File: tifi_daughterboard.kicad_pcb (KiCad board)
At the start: 2 copper layers, 52.3 x 31.5 mm, 19 parts, among them J1 SSW-110-23-F-D, J2 SSW-110-23-F-D, J3 SM04B-SRSS-TB(LF)(SN), J4 SSW-103-02-T-S-RA, Q1 BSS138LT1G, U1 SGP40-D-R4, U2 SHT40-AD1B-R3

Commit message: Routing start
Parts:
- moved R5 8.72 mm to (159.3, 96.4), turned to -90 degrees
- moved D2 7.64 mm to (159.9, 89.7)
- moved Q1 7.64 mm to (156.3, 92.2)
- moved R3 7.64 mm to (156.3, 87.1)
- moved R7 5.45 mm to (131.2, 75.9)
- moved R4 4.64 mm to (160.2, 93.3), turned to 180 degrees
- moved R6 4.48 mm to (130.3, 73.4), turned to 0 degrees
- moved U1 3.95 mm to (145.1, 82.3)
- moved C3 3.75 mm to (134.0, 98.6), turned to 90 degrees
- moved C1 2.99 mm to (147.9, 83.2)
- moved C2 2.79 mm to (141.5, 83.5), turned to 0 degrees
- moved R2 2.51 mm to (142.2, 80.4), turned to -90 degrees
- moved D1 0.13 mm to (159.9, 74.7)
- turned U2 to 0 degrees
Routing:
- net +5V: track 0.00 -> 57.0 mm
- net +3.3V: track 0.00 -> 55.5 mm
- net I2C_SCL: track 17.5 -> 46.4 mm
- net I2C_SDA: track 10.3 -> 38.4 mm
- net LDR_OUT: track 0.00 -> 12.1 mm, vias 0 -> 2
- net Net-(Q1-Pad2): track 0.00 -> 7.02 mm
- net GND: track 0.00 -> 6.17 mm, vias 0 -> 1
- net Net-(U1-Pad1): track 0.00 -> 5.17 mm
- net Net-(D2-Pad2): track 0.00 -> 3.88 mm
- net Net-(D2-Pad1): track 0.00 -> 2.74 mm
- net Net-(D1-Pad2): track 0.00 -> 2.65 mm
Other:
- board size 52.3 x 31.5 mm -> 57.4 x 32.1 mm

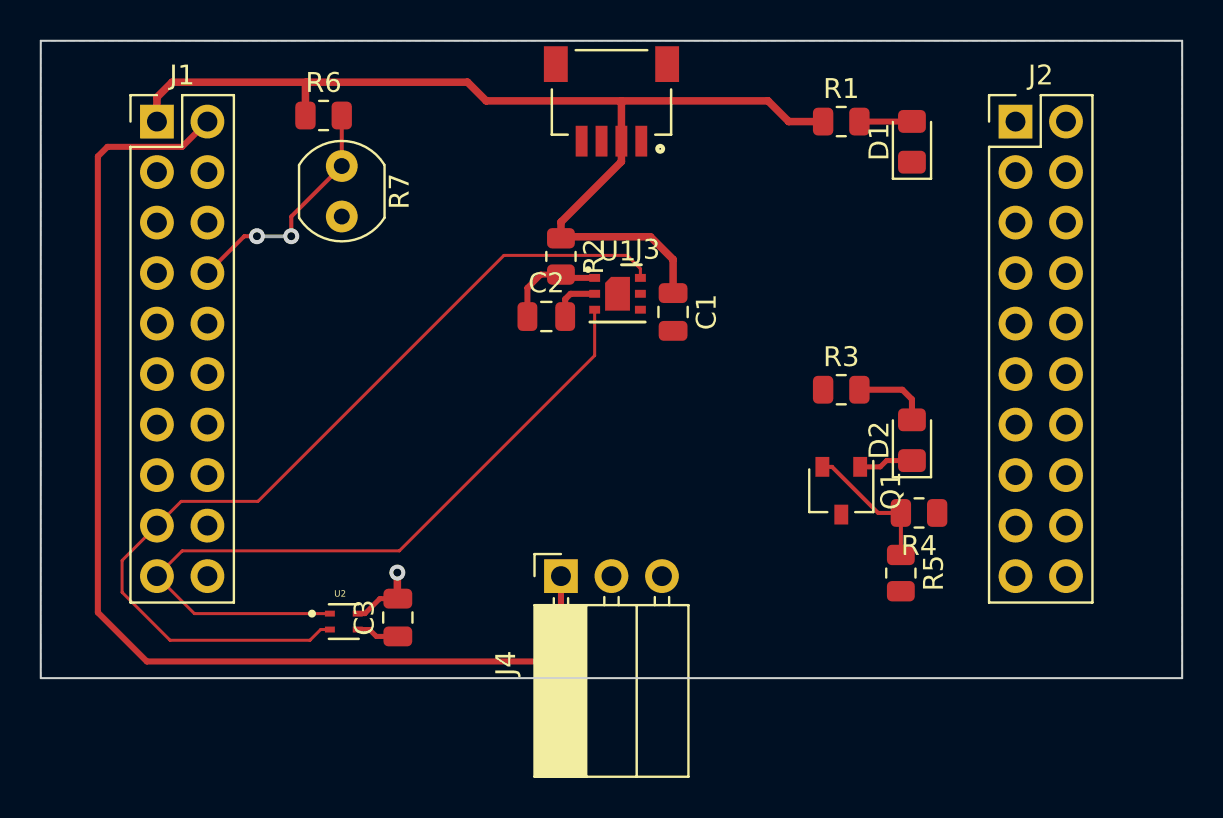
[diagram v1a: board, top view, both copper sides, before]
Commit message: Complete routing, still some TODOs.
TODOS include:
Test pads / points
Reduce vias on I2C signals?
TVS diodes on connectors
Shunt option for blue LED (bypass PWM)
Optional I2C pullups
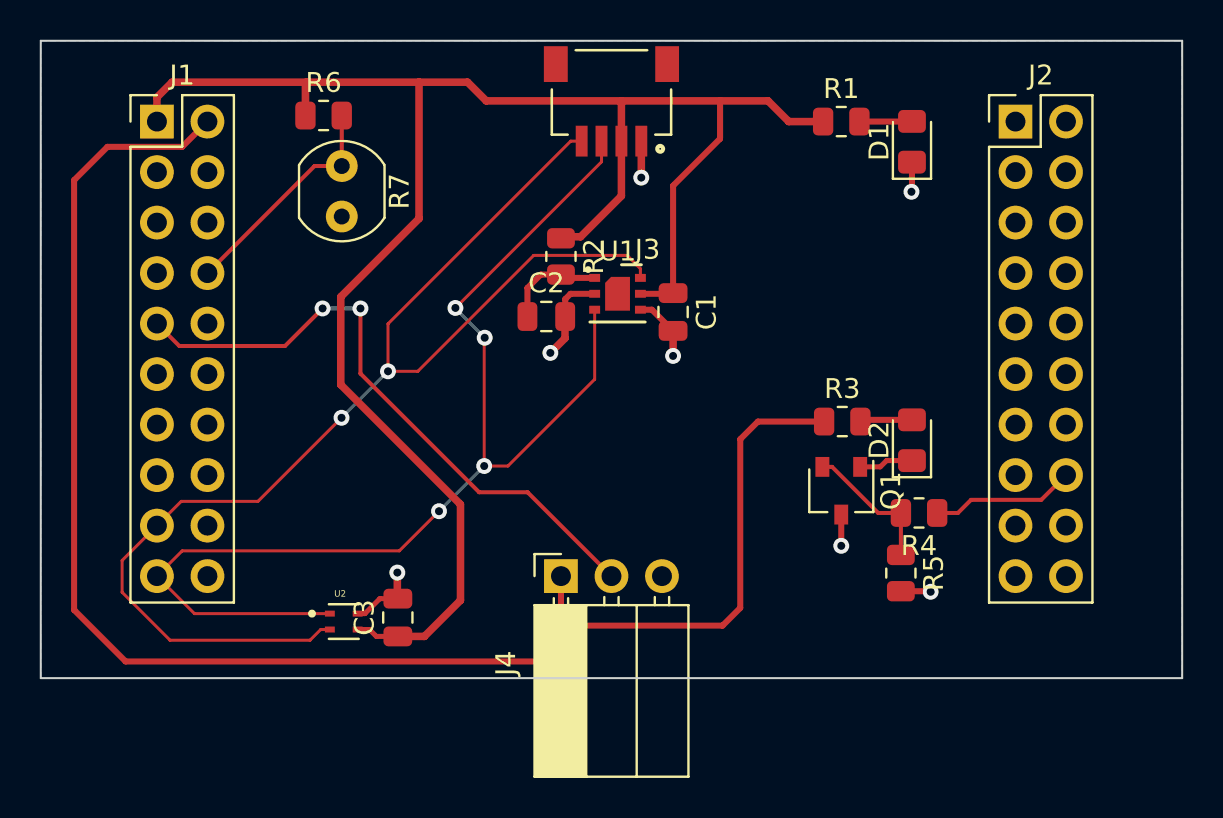
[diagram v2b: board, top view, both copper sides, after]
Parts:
- moved R3 1.60 mm to (156.4, 88.7)
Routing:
- net +3.3V: track 55.5 -> 94.7 mm
- net PIR_OUT: track 0.00 -> 31.6 mm, vias 0 -> 2
- net +5V: track 57.0 -> 81.1 mm
- net I2C_SDA: track 38.4 -> 59.1 mm, vias 0 -> 4
- net I2C_SCL: track 46.4 -> 62.4 mm, vias 0 -> 2
- net GND: track 6.17 -> 18.1 mm, vias 1 -> 7
- net LED_PWM: track 0.00 -> 7.27 mm
- net Net-(D2-Pad2): track 3.88 -> 2.63 mm
- net LDR_OUT: track 12.1 -> 11.5 mm, vias 2 -> 0

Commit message: Move to 4-layer stackup.
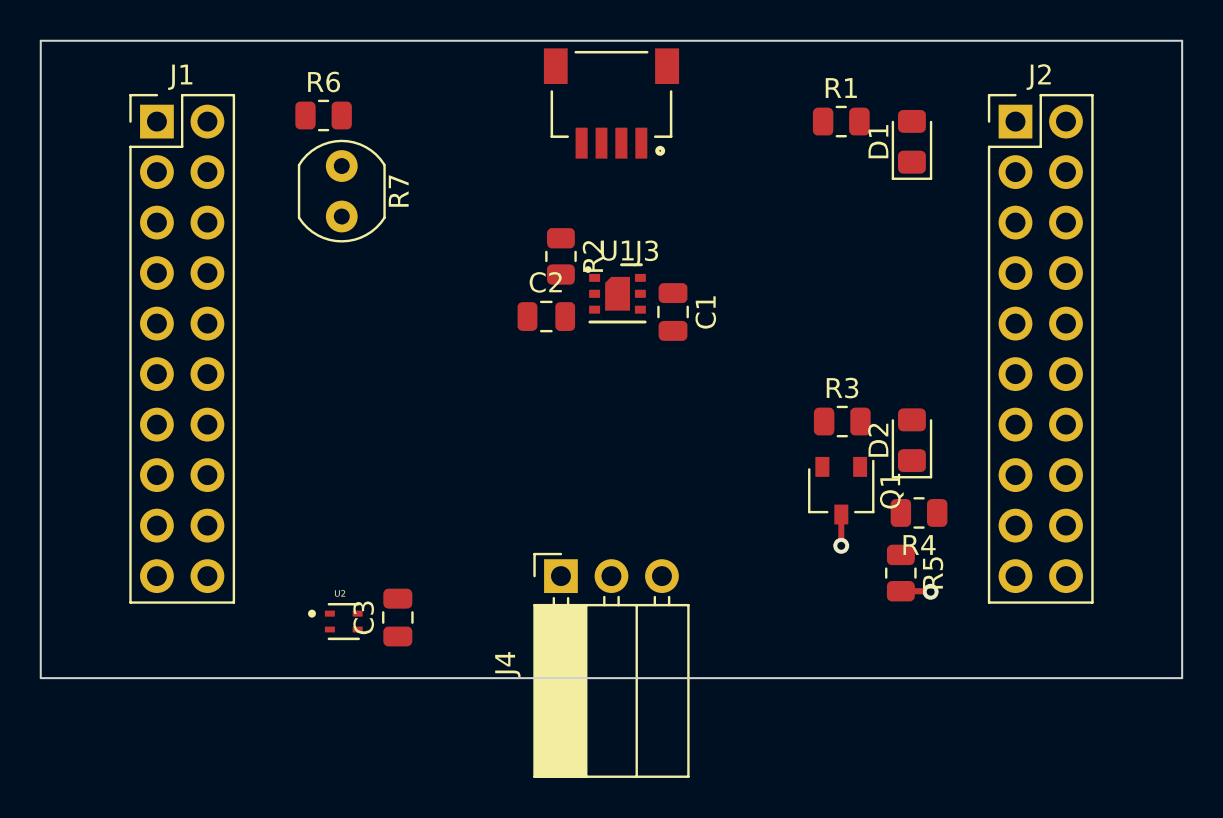
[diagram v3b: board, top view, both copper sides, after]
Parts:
- moved J3 0.10 mm to (144.8, 74.7)
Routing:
- net +3.3V: track 94.7 -> 0.00 mm
- net +5V: track 81.1 -> 0.00 mm
- net I2C_SCL: track 62.4 -> 0.00 mm, vias 2 -> 0
- net I2C_SDA: track 59.1 -> 0.00 mm, vias 4 -> 0
- net PIR_OUT: track 31.6 -> 0.00 mm, vias 2 -> 0
- net GND: track 18.1 -> 3.08 mm, vias 7 -> 2
- net LDR_OUT: track 11.5 -> 0.00 mm
- net LED_PWM: track 7.27 -> 0.00 mm
- net Net-(Q1-Pad2): track 7.02 -> 0.00 mm
- net Net-(U1-Pad1): track 5.17 -> 0.00 mm
- net Net-(D2-Pad1): track 2.74 -> 0.00 mm
- net Net-(D1-Pad2): track 2.65 -> 0.00 mm
- net Net-(D2-Pad2): track 2.63 -> 0.00 mm
- removed copper zone on B.Cu, net GND
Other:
- copper layers 2 -> 4

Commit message: Start 4-layer routing.
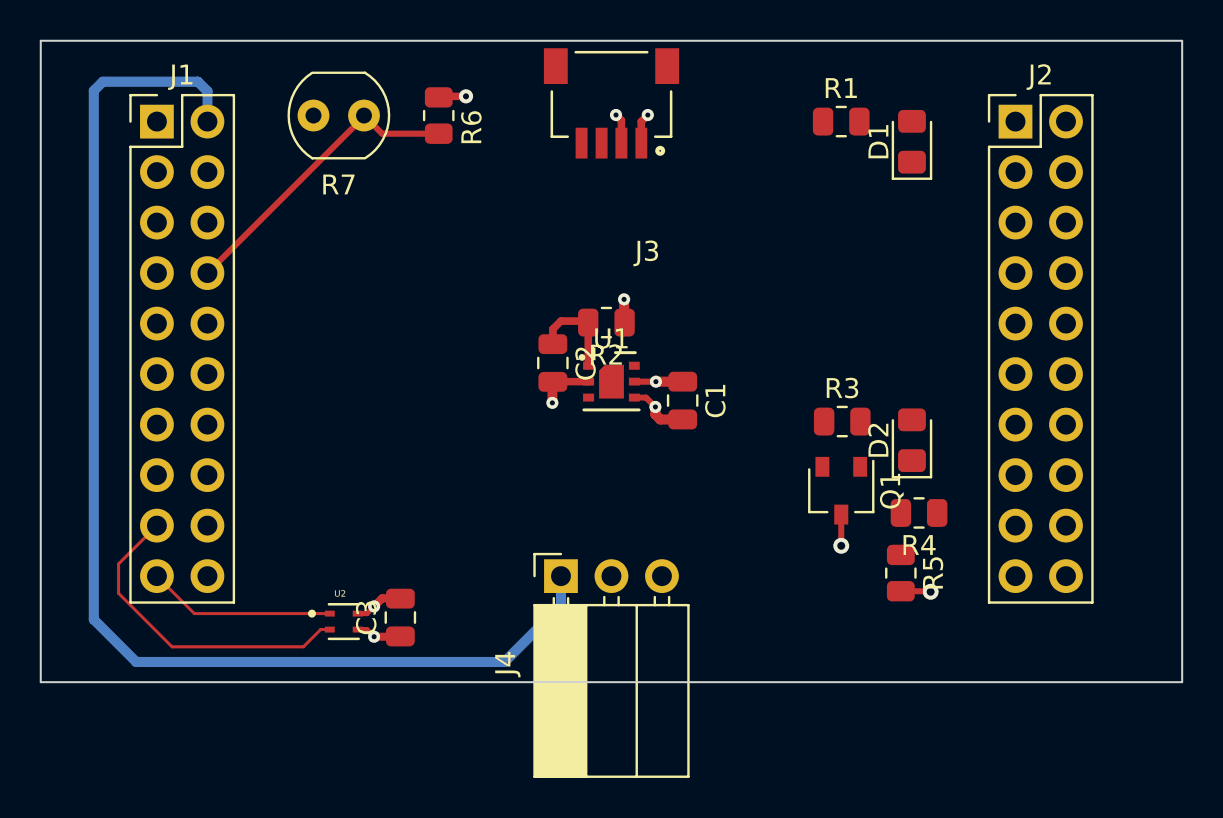
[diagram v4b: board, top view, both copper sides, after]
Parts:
- moved R6 5.79 mm to (136.1, 73.4), turned to -90 degrees
- moved C1 4.48 mm to (148.4, 87.7)
- moved U1 4.43 mm to (144.8, 86.7)
- moved R2 4.04 mm to (144.5, 83.8), turned to 180 degrees
- moved R7 2.78 mm to (132.3, 73.4), turned to 180 degrees
- moved C2 2.36 mm to (141.8, 85.8), turned to -90 degrees
- moved C3 0.13 mm to (134.2, 98.6)
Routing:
- net +5V: track 0.00 -> 61.3 mm
- net I2C_SCL: track 0.00 -> 16.3 mm
- net LDR_OUT: track 0.00 -> 15.3 mm
- net GND: track 3.08 -> 13.1 mm, vias 2 -> 6
- net I2C_SDA: track 0.00 -> 9.48 mm
- net +3.3V: track 0.00 -> 8.98 mm, vias 0 -> 5
- net Net-(U1-Pad1): track 0.00 -> 5.20 mm
- added copper zone on In2.Cu, net +3.3V
- added copper zone on In1.Cu, net GND
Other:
- board size 57.4 x 32.1 mm -> 57.4 x 32.3 mm

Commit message: Revert to two layers. Move PIR sensor output.
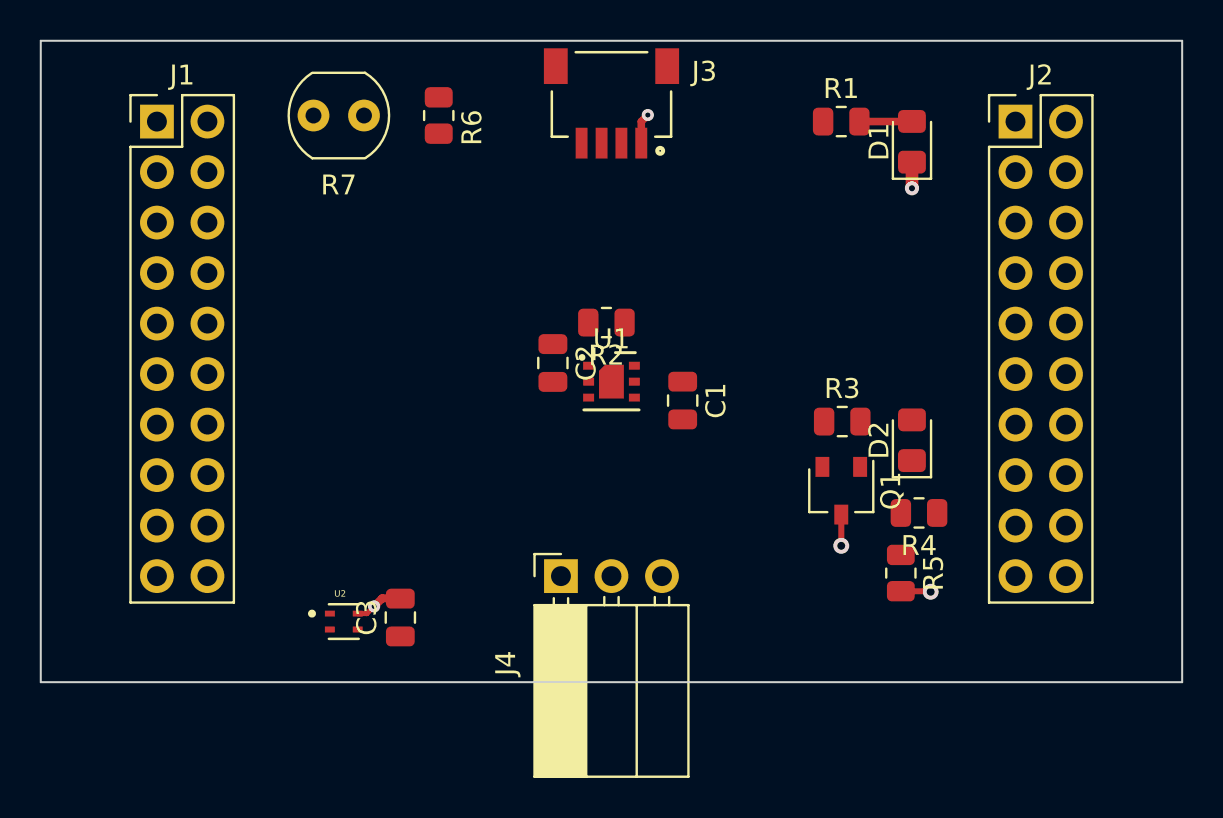
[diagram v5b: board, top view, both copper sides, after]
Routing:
- net +5V: track 61.3 -> 0.00 mm
- net I2C_SCL: track 16.3 -> 0.00 mm
- net LDR_OUT: track 15.3 -> 0.00 mm
- net I2C_SDA: track 9.48 -> 0.00 mm
- net +3.3V: track 8.98 -> 0.00 mm, vias 5 -> 0
- net Net-(U1-Pad1): track 5.20 -> 0.29 mm
- net GND: track 13.1 -> 8.41 mm, vias 6 -> 5
- net Net-(D1-Pad2): track 0.00 -> 2.65 mm
- removed copper zone on In2.Cu, net +3.3V
- removed copper zone on In1.Cu, net GND
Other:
- copper layers 4 -> 2

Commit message: Reposition STEMMA QT to bottom of board.
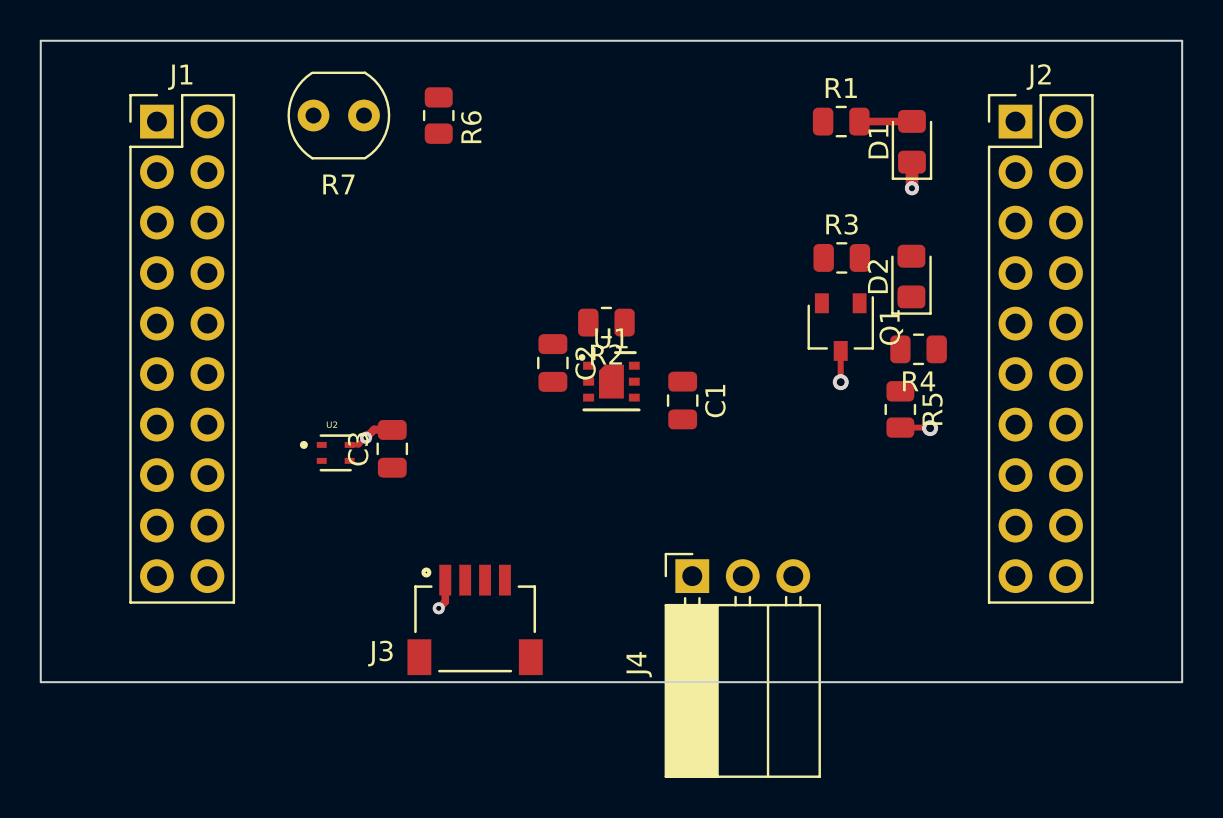
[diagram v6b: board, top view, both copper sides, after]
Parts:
- moved J3 23.0 mm to (137.9, 96.7), turned to 0 degrees
- moved U2 8.49 mm to (130.9, 90.3)
- moved C3 8.49 mm to (133.8, 90.1)
- moved D2 8.23 mm to (159.9, 81.5)
- moved R3 8.23 mm to (156.4, 80.5)
- moved R4 8.23 mm to (160.2, 85.1)
- moved Q1 8.23 mm to (156.3, 84.0)
- moved R5 8.23 mm to (159.3, 88.1)
- moved J4 6.60 mm to (148.8, 96.5)
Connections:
- J1 pad 9: PIR_OUT -> unconnected-(J1-Pad9)
- J2 pad 4: unconnected-(J2-Pad4) -> PIR_OUT
